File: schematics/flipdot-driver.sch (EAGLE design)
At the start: 25 parts, among them IC1 4094D, IC10 4094D, IC11 ULN2003AD, IC12 ULN2003AD, IC13 ULN2003AD, IC14 ULN2003AD, IC15 ULN2003AD, IC16 ULN2003AD, IC17 74HC08D, IC18 74HC08D, IC19 74HC02D, IC2 4094D, IC20 74HC14D, IC21 74HC74D, IC3 4094D, IC4 4094D, IC5 4094D, IC6 4094D, IC7 4094D, IC8 4094D, IC9 4094D

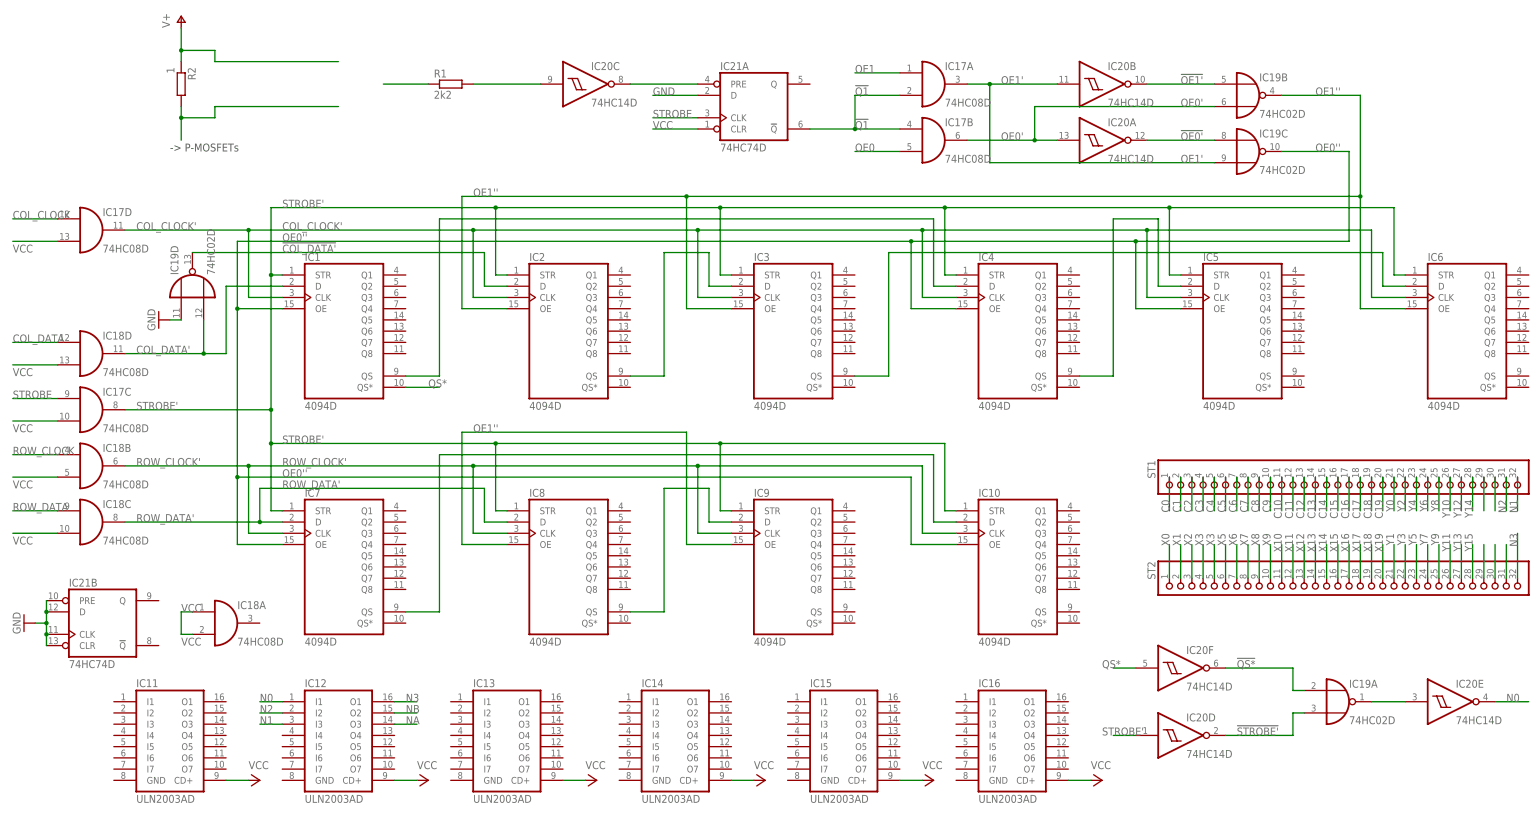
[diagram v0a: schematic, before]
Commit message: swapped 74HC4094 QS1 / QS2
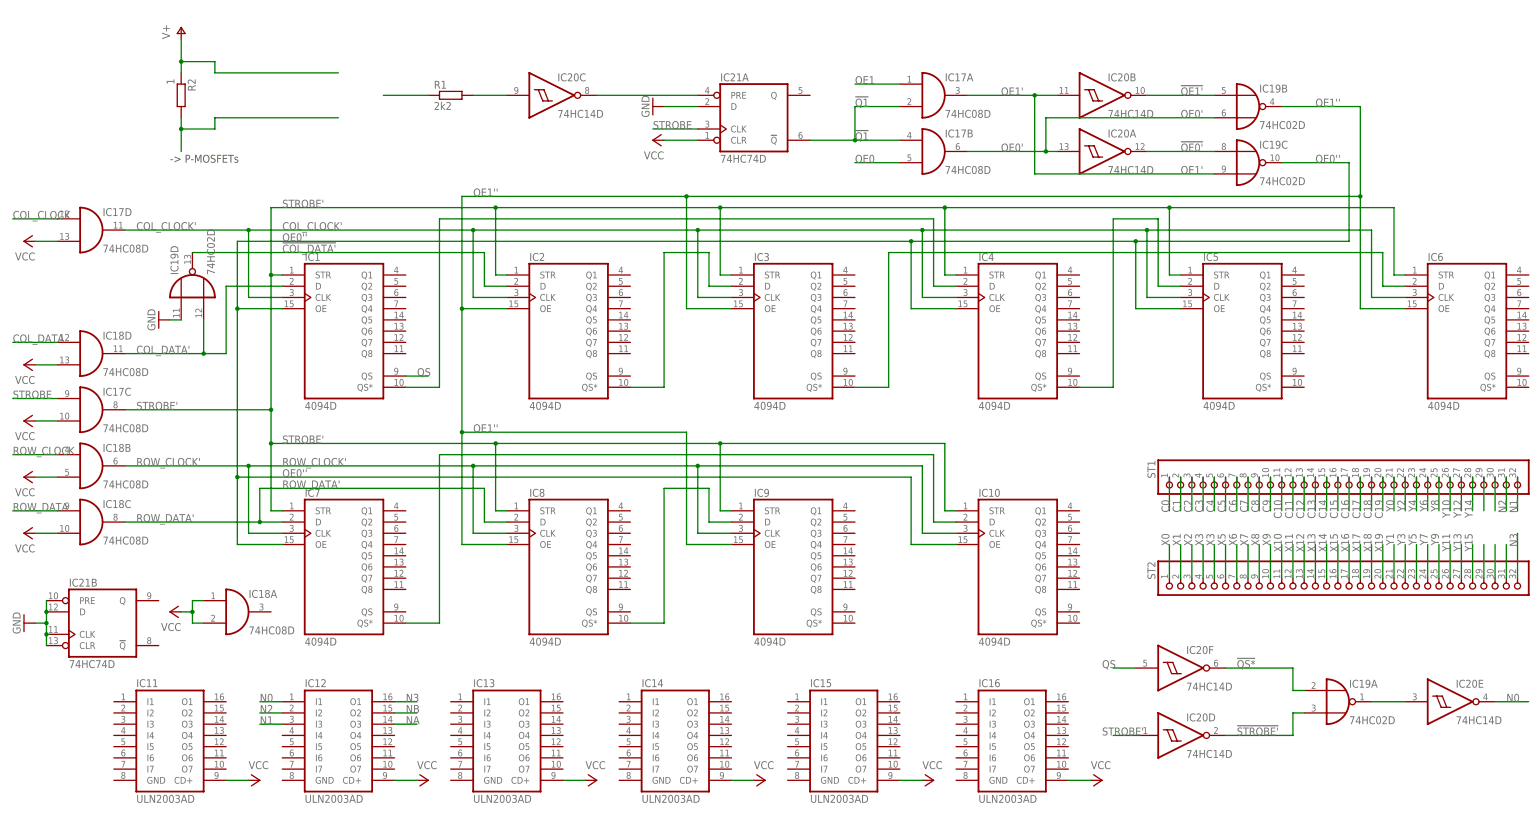
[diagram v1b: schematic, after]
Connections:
- removed net QS*: IC1A.QS*, IC20F.I
- new net QS: IC1A.QS, IC20F.I
- net N$1: now also IC7A.QS*; no longer IC7A.QS
- net N$4: now also IC8A.QS*; no longer IC8A.QS
- net N$5: now also IC1A.QS*; no longer IC1A.QS
- net N$6: now also IC4A.QS*; no longer IC4A.QS
- net N$7: now also IC2A.QS*; no longer IC2A.QS
- net N$9: now also IC3A.QS*; no longer IC3A.QS
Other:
- moved on the sheet: IC17A, IC17B, IC18A, IC19B, IC19C, IC20A, IC20B, IC20C, IC21A, R1, R2

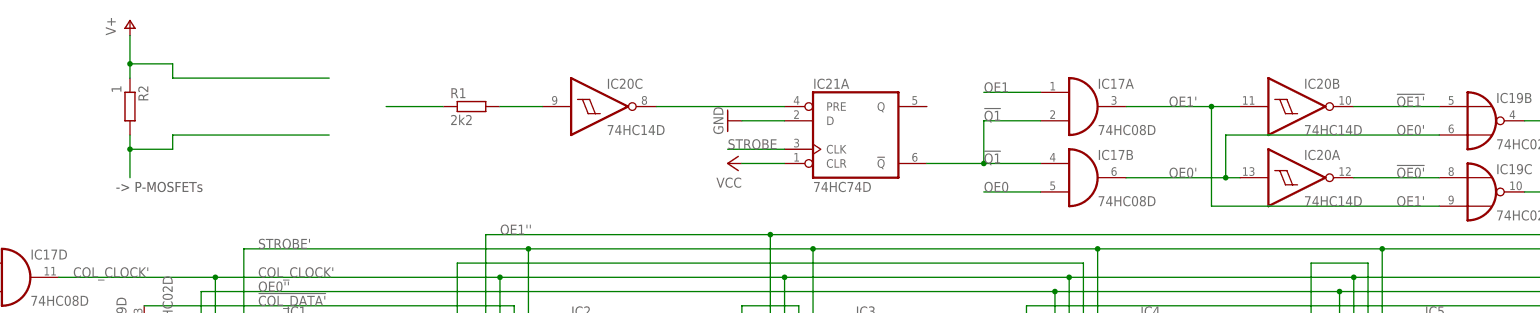
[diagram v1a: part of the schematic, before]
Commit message: updated schematics
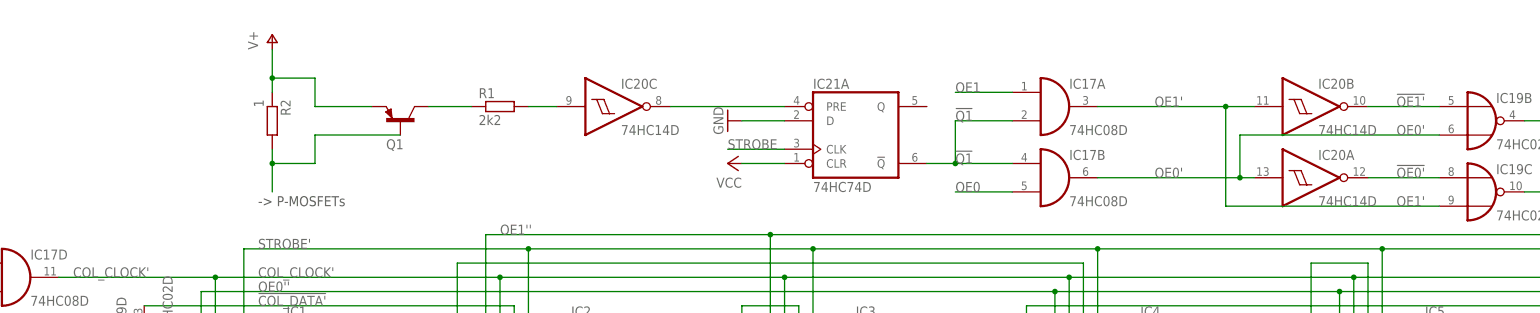
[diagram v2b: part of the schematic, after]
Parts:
- added Q1: BC808-25SMD, transistor-pnp:BC808-25SMD
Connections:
- net N$2: now also Q1.B
- net N$3: now also Q1.C
- net V+: now also Q1.E
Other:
- moved on the sheet: IC17A, IC17B, IC20A, IC20B, IC20C, R1, R2
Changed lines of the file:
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@@
 <part name="GND3" library="supply1" deviceset="GND" device=""/>
 <part name="P+14" library="supply1" deviceset="VCC" device=""/>
+<part name="Q1" library="transistor-pnp" deviceset="BC808*" device="SMD" technology="-25" value=""/>
 </parts>
 <sheets>
 <sheet>
 <plain>
-<text x="35.56" y="144.78" size="1.778" layer="97">-&gt; P-MOSFETs</text>
+<text x="60.96" y="142.24" size="1.778" layer="97">-&gt; P-MOSFETs</text>
 </plain>
 <instances>
@@
 <instance part="IC15" gate="A" x="187.96" y="15.24"/>
 <instance part="IC16" gate="A" x="226.06" y="15.24"/>
-<instance part="IC17" gate="A" x="208.28" y="160.02"/>
-<instance part="IC17" gate="B" x="208.28" y="147.32"/>
+<instance part="IC17" gate="A" x="203.2" y="160.02"/>
+<instance part="IC17" gate="B" x="203.2" y="147.32"/>
 <instance part="IC17" gate="C" x="17.78" y="88.9"/>
 <instance part="IC17" gate="D" x="17.78" y="129.54"/>
@@
 <instance part="IC19" gate="C" x="279.4" y="144.78"/>
 <instance part="IC19" gate="D" x="40.64" y="116.84" rot="R90"/>
-<instance part="IC20" gate="A" x="246.38" y="147.32"/>
-<instance part="IC20" gate="B" x="246.38" y="160.02"/>
-<instance part="IC20" gate="C" x="121.92" y="160.02"/>
+<instance part="IC20" gate="A" x="248.92" y="147.32"/>
+<instance part="IC20" gate="B" x="248.92" y="160.02"/>
+<instance part="IC20" gate="C" x="124.46" y="160.02"/>
 <instance part="IC20" gate="D" x="264.16" y="15.24"/>
 <instance part="IC20" gate="E" x="325.12" y="22.86"/>
@@
 <instance part="IC21" gate="B" x="20.32" y="40.64"/>
 <instance part="GND1" gate="1" x="2.54" y="40.64" rot="R270"/>
-<instance part="R1" gate="G$1" x="99.06" y="160.02"/>
-<instance part="P+7" gate="1" x="38.1" y="175.26"/>
-<instance part="R2" gate="G$1" x="38.1" y="160.02" rot="R270"/>
+<instance part="R1" gate="G$1" x="104.14" y="160.02"/>
+<instance part="P+7" gate="1" x="63.5" y="172.72"/>
+<instance part="R2" gate="G$1" x="63.5" y="157.48" rot="R270"/>
 <instance part="GND2" gate="1" x="33.02" y="109.22" rot="R270"/>
 <instance part="P+8" gate="VCC" x="2.54" y="127" rot="R90"/>
@@
 <instance part="GND3" gate="1" x="144.78" y="157.48" rot="R270"/>
 <instance part="P+14" gate="VCC" x="144.78" y="149.86" rot="R90"/>
+<instance part="Q1" gate="G$1" x="86.36" y="157.48" smashed="yes" rot="R90">
+<attribute name="NAME" x="83.82" y="152.4" size="1.778" layer="95"/>
+<attribute name="VALUE" x="81.28" y="147.32" size="1.778" layer="96" rot="R90"/>
+</instance>
 </instances>
 <busses>
@@
 <segment>
 <pinref part="IC17" gate="A" pin="I0"/>
-<wire x1="200.66" y1="162.56" x2="190.5" y2="162.56" width="0.1524" layer="91"/>
-<label x="190.5" y="162.56" size="1.778" layer="95"/>
+<wire x1="195.58" y1="162.56" x2="185.42" y2="162.56" width="0.1524" layer="91"/>
+<label x="185.42" y="162.56" size="1.778" layer="95"/>
 </segment>
 </net>
@@
 <segment>
 <pinref part="IC17" gate="B" pin="I1"/>
-<wire x1="200.66" y1="144.78" x2="190.5" y2="144.78" width="0.1524" layer="91"/>
-<label x="190.5" y="144.78" size="1.778" layer="95"/>
+<wire x1="195.58" y1="144.78" x2="185.42" y2="144.78" width="0.1524" layer="91"/>
+<label x="185.42" y="144.78" size="1.778" layer="95"/>
 </segment>
 </net>
@@
 <pinref part="IC20" gate="A" pin="I"/>
 <pinref part="IC17" gate="B" pin="O"/>
-<wire x1="215.9" y1="147.32" x2="233.68" y2="147.32" width="0.1524" layer="91"/>
-<label x="223.52" y="147.32" size="1.778" layer="95"/>
+<wire x1="210.82" y1="147.32" x2="236.22" y2="147.32" width="0.1524" layer="91"/>
+<label x="220.98" y="147.32" size="1.778" layer="95"/>
 <pinref part="IC19" gate="B" pin="I1"/>
-<wire x1="233.68" y1="147.32" x2="236.22" y2="147.32" width="0.1524" layer="91"/>
+<wire x1="236.22" y1="147.32" x2="238.76" y2="147.32" width="0.1524" layer="91"/>
 <label x="264.16" y="154.94" size="1.778" layer="95"/>
-<wire x1="233.68" y1="147.32" x2="233.68" y2="154.94" width="0.1524" layer="91"/>
-<wire x1="233.68" y1="154.94" x2="271.78" y2="154.94" width="0.1524" layer="91"/>
-<junction x="233.68" y="147.32"/>
+<wire x1="236.22" y1="147.32" x2="236.22" y2="154.94" width="0.1524" layer="91"/>
+<wire x1="236.22" y1="154.94" x2="271.78" y2="154.94" width="0.1524" layer="91"/>
+<junction x="236.22" y="147.32"/>
 </segment>
 </net>
@@
 <segment>
 <pinref part="IC17" gate="A" pin="O"/>
-<wire x1="215.9" y1="160.02" x2="231.14" y2="160.02" width="0.1524" layer="91"/>
-<label x="223.52" y="160.02" size="1.778" layer="95"/>
+<wire x1="210.82" y1="160.02" x2="233.68" y2="160.02" width="0.1524" layer="91"/>
+<label x="220.98" y="160.02" size="1.778" layer="95"/>
 <pinref part="IC20" gate="B" pin="I"/>
 <pinref part="IC19" gate="C" pin="I1"/>
-<wire x1="231.14" y1="160.02" x2="236.22" y2="160.02" width="0.1524" layer="91"/>
+<wire x1="233.68" y1="160.02" x2="238.76" y2="160.02" width="0.1524" layer="91"/>
 <label x="264.16" y="142.24" size="1.778" layer="95"/>
-<wire x1="231.14" y1="160.02" x2="231.14" y2="142.24" width="0.1524" layer="91"/>
-<wire x1="231.14" y1="142.24" x2="271.78" y2="142.24" width="0.1524" layer="91"/>
-<junction x="231.14" y="160.02"/>
+<wire x1="233.68" y1="160.02" x2="233.68" y2="142.24" width="0.1524" layer="91"/>
+<wire x1="233.68" y1="142.24" x2="271.78" y2="142.24" width="0.1524" layer="91"/>
+<junction x="233.68" y="160.02"/>
 </segment>
 </net>
@@
 <segment>
 <pinref part="IC17" gate="B" pin="I0"/>
-<label x="190.5" y="149.86" size="1.778" layer="95"/>
+<label x="185.42" y="149.86" size="1.778" layer="95"/>
 <pinref part="IC17" gate="A" pin="I1"/>
-<wire x1="190.5" y1="149.86" x2="200.66" y2="149.86" width="0.1524" layer="91"/>
-<wire x1="200.66" y1="157.48" x2="190.5" y2="157.48" width="0.1524" layer="91"/>
-<label x="190.5" y="157.48" size="1.778" layer="95"/>
-<wire x1="190.5" y1="149.86" x2="190.5" y2="157.48" width="0.1524" layer="91"/>
+<wire x1="185.42" y1="149.86" x2="195.58" y2="149.86" width="0.1524" layer="91"/>
+<wire x1="195.58" y1="157.48" x2="185.42" y2="157.48" width="0.1524" layer="91"/>
+<label x="185.42" y="157.48" size="1.778" layer="95"/>
+<wire x1="185.42" y1="149.86" x2="185.42" y2="157.48" width="0.1524" layer="91"/>
 <pinref part="IC21" gate="A" pin="!Q"/>
-<wire x1="190.5" y1="149.86" x2="180.34" y2="149.86" width="0.1524" layer="91"/>
-<junction x="190.5" y="149.86"/>
+<wire x1="185.42" y1="149.86" x2="180.34" y2="149.86" width="0.1524" layer="91"/>
+<junction x="185.42" y="149.86"/>
 </segment>
 </net>
@@
 <pinref part="IC21" gate="A" pin="PRE"/>
 <pinref part="IC20" gate="C" pin="O"/>
-<wire x1="132.08" y1="160.02" x2="154.94" y2="160.02" width="0.1524" layer="91"/>
+<wire x1="134.62" y1="160.02" x2="154.94" y2="160.02" width="0.1524" layer="91"/>
 </segment>
 </net>
@@
 <segment>
 <pinref part="IC20" gate="C" pin="I"/>
-<wire x1="111.76" y1="160.02" x2="104.14" y2="160.02" width="0.1524" layer="91"/>
+<wire x1="114.3" y1="160.02" x2="109.22" y2="160.02" width="0.1524" layer="91"/>
 <pinref part="R1" gate="G$1" pin="2"/>
 </segment>
@@
 <label x="264.16" y="147.32" size="1.778" layer="95"/>
 <pinref part="IC19" gate="C" pin="I0"/>
-<wire x1="271.78" y1="147.32" x2="256.54" y2="147.32" width="0.1524" layer="91"/>
+<wire x1="271.78" y1="147.32" x2="259.08" y2="147.32" width="0.1524" layer="91"/>
 </segment>
 </net>
@@
 <segment>
 <pinref part="IC20" gate="B" pin="O"/>
-<wire x1="256.54" y1="160.02" x2="271.78" y2="160.02" width="0.1524" layer="91"/>
+<wire x1="259.08" y1="160.02" x2="271.78" y2="160.02" width="0.1524" layer="91"/>
 <label x="264.16" y="160.02" size="1.778" layer="95"/>
 <pinref part="IC19" gate="B" pin="I0"/>
@@
 <pinref part="P+7" gate="1" pin="V+"/>
 <pinref part="R2" gate="G$1" pin="1"/>
-<wire x1="38.1" y1="165.1" x2="38.1" y2="167.64" width="0.1524" layer="91"/>
-<wire x1="38.1" y1="167.64" x2="38.1" y2="172.72" width="0.1524" layer="91"/>
-<wire x1="38.1" y1="167.64" x2="45.72" y2="167.64" width="0.1524" layer="91"/>
-<wire x1="45.72" y1="167.64" x2="45.72" y2="165.1" width="0.1524" layer="91"/>
-<junction x="38.1" y="167.64"/>
-<wire x1="45.72" y1="165.1" x2="73.66" y2="165.1" width="0.1524" layer="91"/>
+<wire x1="63.5" y1="162.56" x2="63.5" y2="165.1" width="0.1524" layer="91"/>
+<wire x1="63.5" y1="165.1" x2="63.5" y2="170.18" width="0.1524" layer="91"/>
+<wire x1="63.5" y1="165.1" x2="71.12" y2="165.1" width="0.1524" layer="91"/>
+<wire x1="71.12" y1="165.1" x2="71.12" y2="160.02" width="0.1524" layer="91"/>
+<junction x="63.5" y="165.1"/>
+<wire x1="71.12" y1="160.02" x2="81.28" y2="160.02" width="0.1524" layer="91"/>
+<pinref part="Q1" gate="G$1" pin="E"/>
 </segment>
 </net>
@@
 <segment>
 <pinref part="R1" gate="G$1" pin="1"/>
-<wire x1="93.98" y1="160.02" x2="83.82" y2="160.02" width="0.1524" layer="91"/>
+<wire x1="99.06" y1="160.02" x2="91.44" y2="160.02" width="0.1524" layer="91"/>
+<pinref part="Q1" gate="G$1" pin="C"/>
 </segment>
 </net>
@@
 <segment>
 <pinref part="R2" gate="G$1" pin="2"/>
-<wire x1="38.1" y1="154.94" x2="38.1" y2="152.4" width="0.1524" layer="91"/>
-<wire x1="38.1" y1="152.4" x2="38.1" y2="147.32" width="0.1524" layer="91"/>
-<wire x1="38.1" y1="152.4" x2="45.72" y2="152.4" width="0.1524" layer="91"/>
-<wire x1="45.72" y1="152.4" x2="45.72" y2="154.94" width="0.1524" layer="91"/>
-<junction x="38.1" y="152.4"/>
-<wire x1="45.72" y1="154.94" x2="73.66" y2="154.94" width="0.1524" layer="91"/>
-</segment>
-</net>
+<wire x1="63.5" y1="152.4" x2="63.5" y2="149.86" width="0.1524" layer="91"/>
+<wire x1="63.5" y1="149.86" x2="63.5" y2="144.78" width="0.1524" layer="91"/>
+<wire x1="63.5" y1="149.86" x2="71.12" y2="149.86" width="0.1524" layer="91"/>
+<wire x1="71.12" y1="149.86" x2="71.12" y2="154.94" width="0.1524" layer="91"/>
+<junction x="63.5" y="149.86"/>
+<wire x1="71.12" y1="154.94" x2="86.36" y2="154.94" width="0.1524" layer="91"/>
+<pinref part="Q1" gate="G$1" pin="B"/>
+</segment>
+</net>
